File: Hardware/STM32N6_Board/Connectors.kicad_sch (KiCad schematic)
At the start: 11 parts, among them J10 BOOT0, J11 Conn_01x18_Socket, J12 Conn_01x18_Socket, J3 Conn_01x08_Pin, J4 Conn_01x18_Pin, J5 Conn_01x18_Pin, J6 Conn_01x05_Pin, J7 SFW15R-2STE1LF, J8 12401832E402A, J9 BOOT1

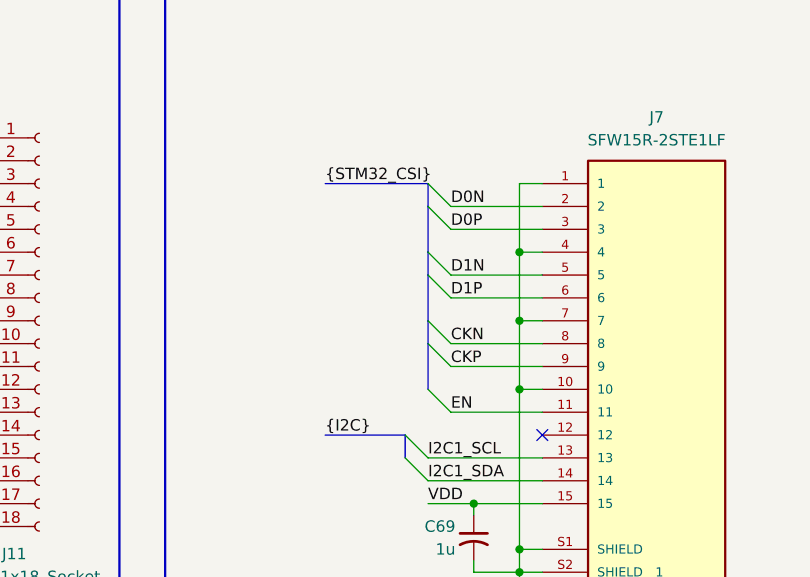
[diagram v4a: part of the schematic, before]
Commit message: Completed a lot of the layout of the STM Board
- Major layout complete, but all the wiring still left. 488 open nets!
- The STM32's BGA fanout is complete, now comes laying out traces
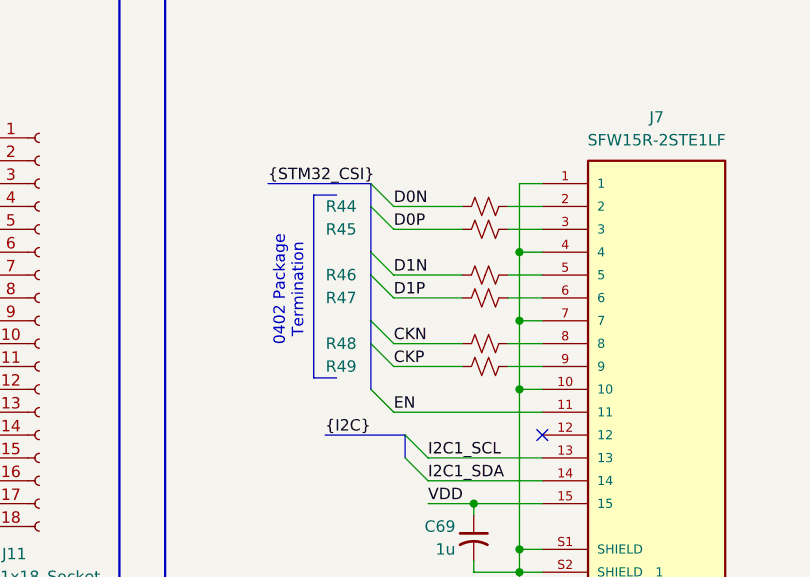
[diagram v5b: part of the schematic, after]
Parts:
- added R44, R45, R46, R47, R48, R49: 0R, Resistor_SMD:R_0402_1005Metric, symbol Device:R_Small_US
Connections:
- net CKN: now also R48.1; no longer J7.8
- net CKP: now also R49.1; no longer J7.9
- net D0N: now also R44.1; no longer J7.2
- net D0P: now also R45.1; no longer J7.3
- net D1N: now also R46.1; no longer J7.5
- net D1P: now also R47.1; no longer J7.6
- new net: J7.3, R45.2
- new net: J7.2, R44.2
- new net: J7.5, R46.2
- new net: J7.6, R47.2
- new net: J7.8, R48.2
- new net: J7.9, R49.2
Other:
- note added: "0402 Package Termination"

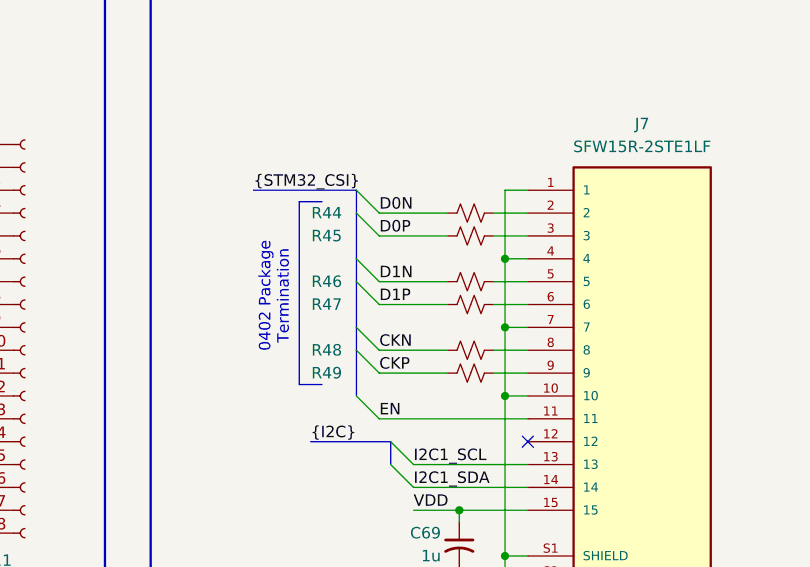
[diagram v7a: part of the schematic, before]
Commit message: added decoupling caps and other stuffs
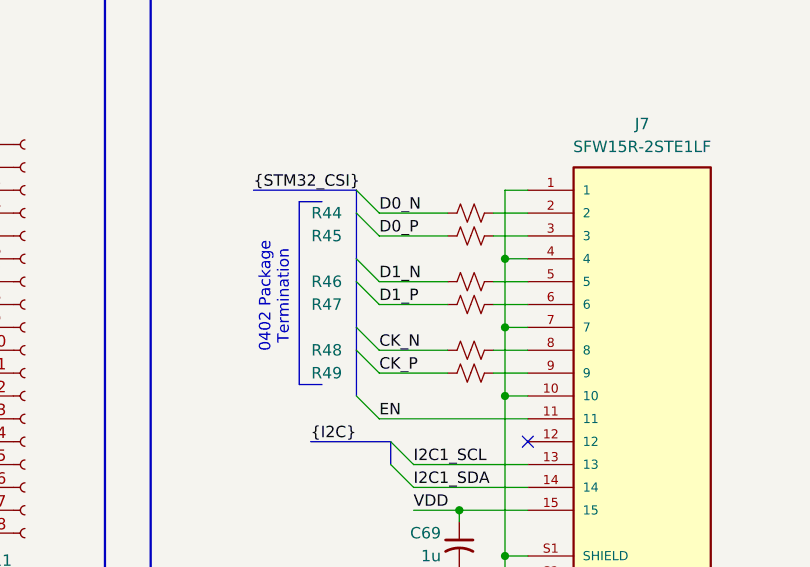
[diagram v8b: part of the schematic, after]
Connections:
- net CKN renamed CK_N
- net CKP renamed CK_P
- net D0N renamed D0_N
- net D0P renamed D0_P
- net D1N renamed D1_N
- net D1P renamed D1_P
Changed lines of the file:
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@@
 		)
 	)
-	(label "CKP"
+	(label "CK_P"
 		(at 149.86 72.39 0)
 		(effects
@@
 		)
 	)
-	(label "CKN"
+	(label "CK_N"
 		(at 149.86 69.85 0)
 		(effects
@@
 		)
 	)
-	(label "D1N"
+	(label "D1_N"
 		(at 149.86 62.23 0)
 		(effects
@@
 		)
 	)
-	(label "D0N"
+	(label "D0_N"
 		(at 149.86 54.61 0)
 		(effects
@@
 		)
 	)
-	(label "D1P"
+	(label "D1_P"
 		(at 149.86 64.77 0)
 		(effects
@@
 		)
 	)
-	(label "D0P"
+	(label "D0_P"
 		(at 149.86 57.15 0)
 		(effects
